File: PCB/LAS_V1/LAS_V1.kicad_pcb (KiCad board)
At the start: 2 copper layers, 69 x 95 mm, 64 parts, among them J1 Screw_Terminal_01x04, J2 Conn_01x03_Pin, J3 Conn_01x05_Socket, J4 Conn_01x22_Socket, J5 Conn_01x22_Socket, J6 Conn_01x02_Pin, J7 USB_C_Receptacle_USB2.0, J8 Conn_01x05, J9 Conn_01x02_Pin, K1 SRD-05VDC-SL-C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

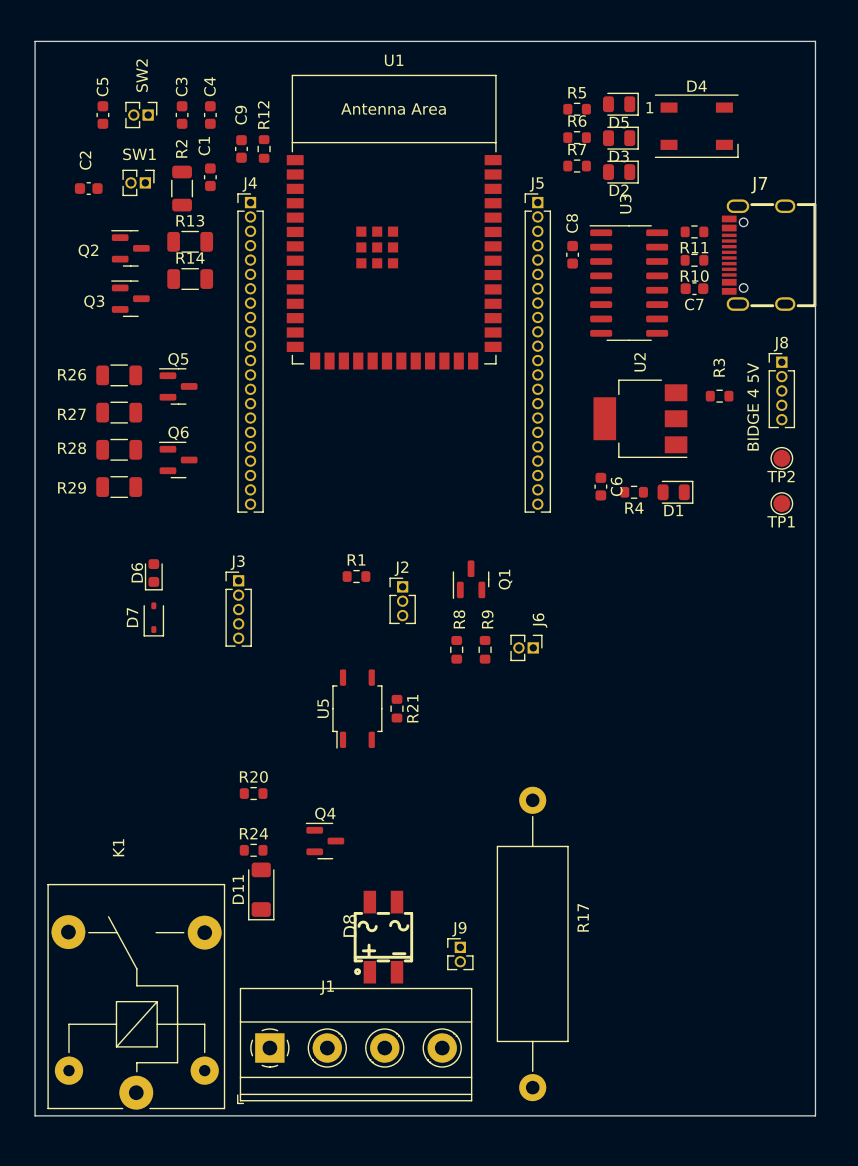
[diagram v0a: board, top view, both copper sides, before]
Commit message: PCB V1 complete
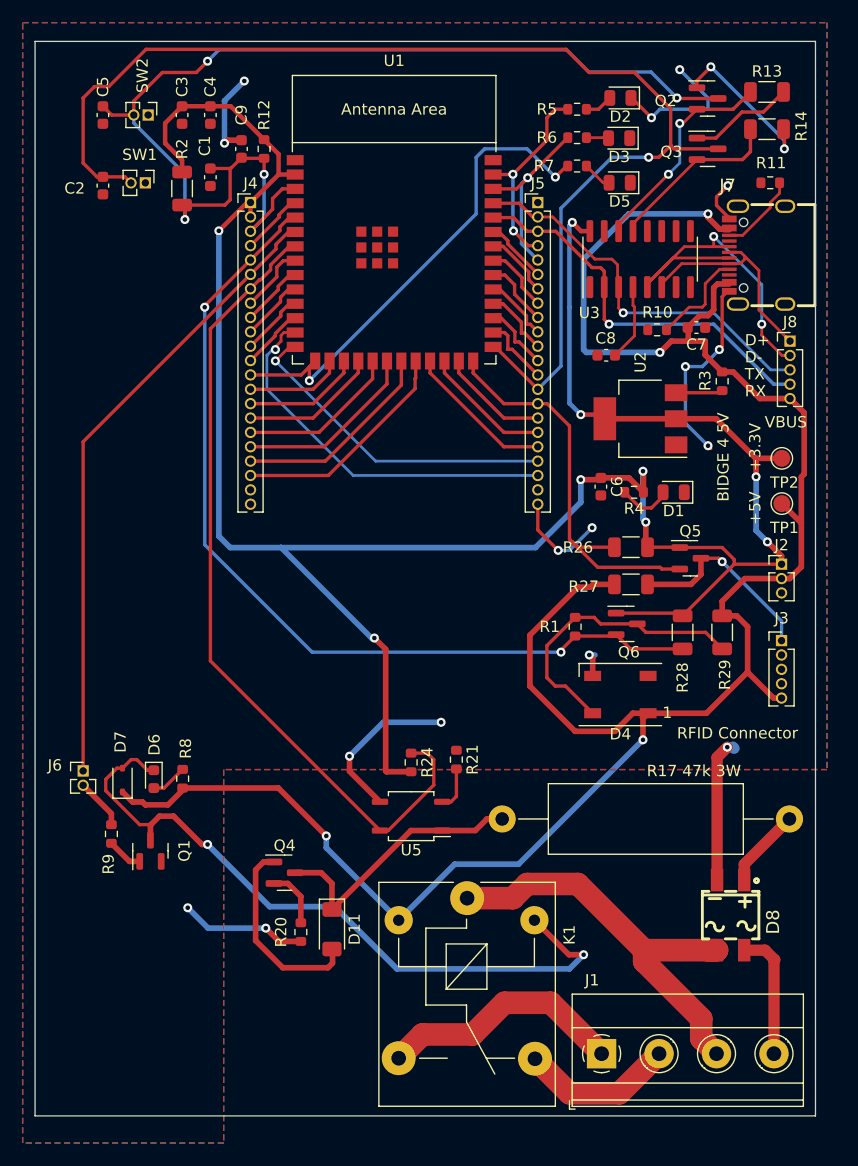
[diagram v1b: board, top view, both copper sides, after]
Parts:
- removed J9: Conn_01x02_Pin, Connector_PinHeader_1.27mm:PinHeader_1x02_P1.27mm_Vertical
- R17 47k 3W: renamed from R17
- moved R29 54.8 mm to (150.8, 107.2), turned to -90 degrees
- moved Q2 52.7 mm to (149.5, 60.0)
- moved Q3 52.7 mm to (149.5, 64.5)
- moved R13 52.7 mm to (154.7, 59.5)
- moved R14 52.7 mm to (154.7, 62.8)
- moved R28 52.4 mm to (147.2, 107.2), turned to -90 degrees
- moved D4 50.7 mm to (141.8, 112.8), turned to 180 degrees
- moved J3 48.3 mm to (156.0, 108.0)
- moved Q5 47.7 mm to (147.9, 100.7)
- moved R26 47.7 mm to (142.7, 99.7), turned to 180 degrees
- moved R27 47.7 mm to (142.7, 103.0)
- moved Q6 42.2 mm to (142.3, 106.5)
- moved J6 41.3 mm to (94.2, 119.5), turned to 0 degrees
- moved Q1 37.1 mm to (100.2, 126.6)
- moved R9 36.8 mm to (96.8, 125.1), turned to -90 degrees
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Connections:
- D8 pad 3: Net-(J9-Pin_1) -> /LIVE
- J1 pad 1: /NEUTRAL -> /N01
- J1 pad 2: /N01 -> /NC1
- J1 pad 3: /NC1 -> /LIVE
- J1 pad 4: /LIVE -> /NEUTRAL
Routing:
- net /+3.3V: track 0.00 -> 207.4 mm, vias 0 -> 9
- net /VBus: track 0.00 -> 190.1 mm, vias 0 -> 4
- net /BOOT_SEL: track 0.00 -> 108.6 mm, vias 0 -> 1
- net /CHIP_PU: track 0.00 -> 97.5 mm, vias 0 -> 4
- net GND: track 0.00 -> 91.5 mm, vias 0 -> 16
- net /DIN_3.3: track 0.00 -> 80.0 mm, vias 0 -> 2
- net /AC_Mon_1: track 0.00 -> 72.2 mm
- net Net-(D6-K): track 0.00 -> 63.3 mm, vias 0 -> 2
- net /GPIO6: track 0.00 -> 55.8 mm
- net /GPIO3: track 0.00 -> 43.9 mm, vias 0 -> 2
- net /LIVE: track 0.00 -> 37.8 mm
- net /GPIO45: track 0.00 -> 36.3 mm
- net /RXD0: track 0.00 -> 34.8 mm, vias 0 -> 1
- net /TXD0: track 0.00 -> 34.2 mm, vias 0 -> 1
- net /GPIO19: track 0.00 -> 33.9 mm, vias 0 -> 1
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- added copper zone on B.Cu, net GND
- added copper zone on F.Cu, net GND
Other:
- board text added: "+3.3V"
- board text added: "+5V"
- board text added: "D+"
- board text added: "D-"
- board text added: "RFID Connector"
- board text added: "RX"
- board text added: "TX"
- board text added: "VBUS"

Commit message: PCBV1 done, moving onto V2
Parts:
- R17: renamed from R17 47k 3W
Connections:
- Q5 pad 2: /GPIO45 -> /GPIO18
- R26 pad 2: /GPIO45 -> /GPIO18
- R7 pad 1: /GPIO3 -> /GPIO4
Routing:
- net /GPIO18: track 5.70 -> 72.4 mm
- net /GPIO3: track 43.9 -> 6.22 mm, vias 2 -> 0
- net /GPIO4: track 5.63 -> 37.8 mm, vias 0 -> 1
- net /GPIO45: track 36.3 -> 7.89 mm
- net GND: track 91.5 -> 98.5 mm
- net /VBus: track 190.1 -> 194.6 mm
- net /LIVE: track 37.8 -> 37.3 mm
